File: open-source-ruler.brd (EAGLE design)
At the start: 85.5 x 54 mm, 30 parts, among them IC1 LT1007CS8, IC2 FT232RLSSOP, IC3 MDC3105DMT1, Q4 ASF1, U1 V_REG_317DPACK

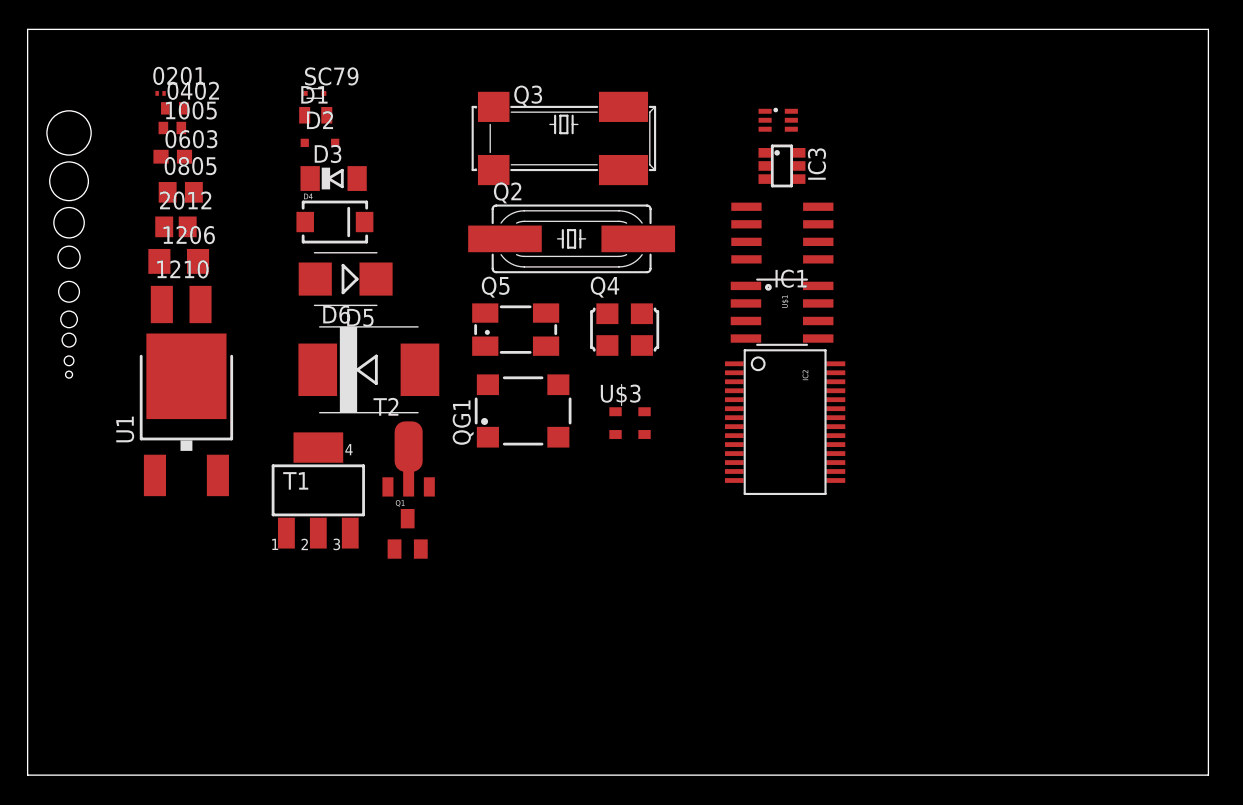
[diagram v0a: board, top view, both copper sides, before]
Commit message: Added scales
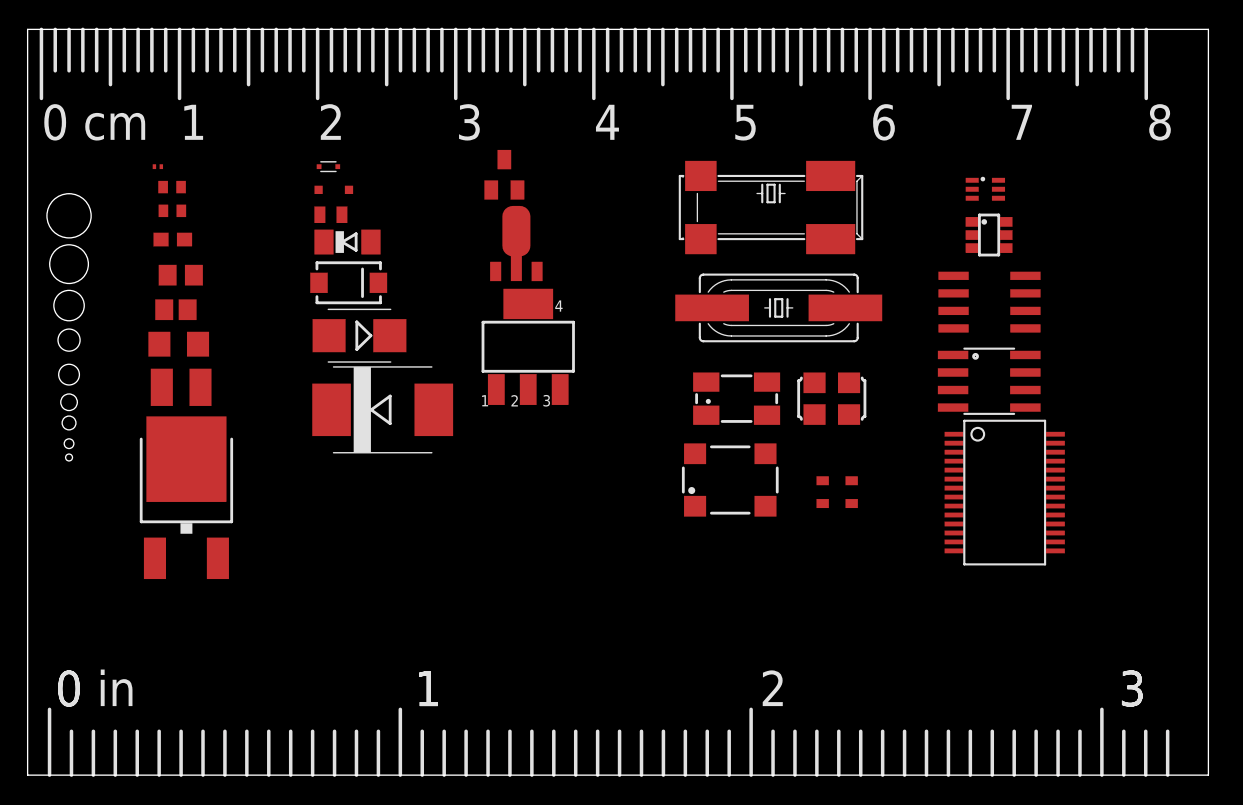
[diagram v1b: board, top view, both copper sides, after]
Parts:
- moved Q1 26.9 mm to (34.5, 43.5)
- moved T1 18.4 mm to (36.2, 31.0)
- moved T2 17.4 mm to (35.4, 38.5)
- moved Q5 16.8 mm to (51.3, 27.3)
- moved IC2 16.7 mm to (70.8, 20.5)
- moved IC1 15.8 mm to (69.7, 34.2)
- moved IC3 15.8 mm to (69.6, 39.1)
- moved Q2 15.8 mm to (54.4, 33.8)
- moved Q3 15.8 mm to (53.8, 41.1)
- moved QG1 15.8 mm to (50.9, 21.4)
- moved U$3 15.8 mm to (58.6, 20.5)
- moved Q4 15.8 mm to (58.2, 27.3)
- moved U$1 15.8 mm to (69.6, 28.5)
- moved U$2 15.8 mm to (69.3, 42.4)
- moved D1 7.28 mm to (22.0, 40.6)
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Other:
- board text added: "0"
- board text added: "1"
- board text added: "2"
- board text added: "3"
- board text added: "4"
- board text added: "5"
- board text added: "6"
- board text added: "7"
- board text added: "8"
- board text added: "cm"
- board text added: "in"

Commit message: Added prototype area
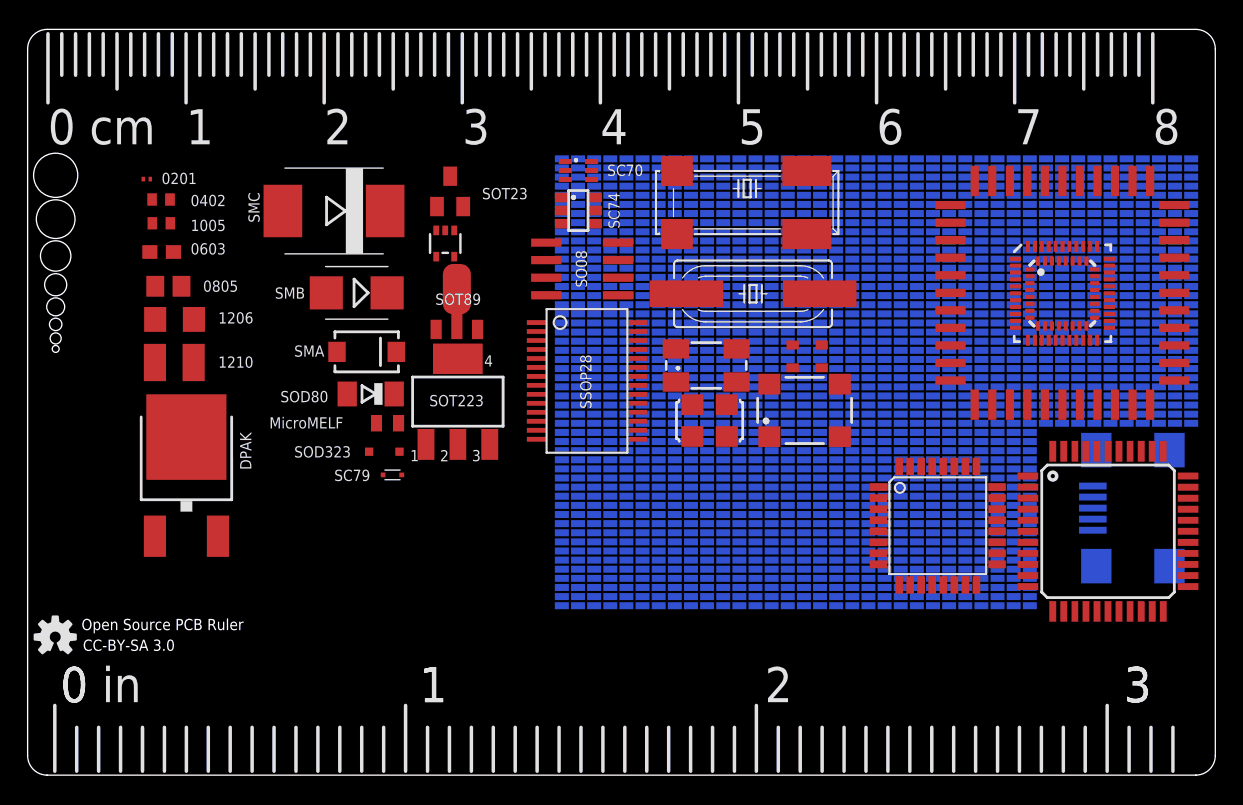
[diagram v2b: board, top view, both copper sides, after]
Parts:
- removed 2012: (no value), rcl:C2012
- added IC4: XMEGA16A4A, atmel:TQFP44
- added IC6: (no value), micro-intel:PLCC44
- added U$10, U$11, U$12, U$13, U$14, U$15, U$16, U$17, U$18, U$19, U$20, U$21, U$22, U$4, U$6, U$7, U$8, U$9: PADS, my:PADS
- added U$5: ATMEGA32U4QFN2, SparkFun:QFN-44-NOPAD
- added U2: ATMEGA168, SparkFun:TQFP32-08
- added U3: ATMEGA168MLF, SparkFun:MLF32
- added U4: 7432SE, SparkFun:SOT353
- added X1: MINI-USB-UX60A-MB-5ST, usb:UX60A-MB-5ST
- U$1: value ATTINY13SOIC -> OSHW-LOGOS; device SparkFun:SO08 -> SparkFun:OSHW-LOGO-S
- moved U$1 70.1 mm to (2.00, 10.0), turned to 0 degrees
- moved IC2 31.3 mm to (40.5, 28.5)
- moved IC3 29.8 mm to (39.9, 40.9)
- moved IC1 29.6 mm to (40.2, 36.7)
- moved U$2 29.5 mm to (39.9, 43.8)
- moved SC79 22.8 mm to (26.4, 21.7), turned to 180 degrees
- moved D2 19.3 mm to (25.8, 23.4), turned to 180 degrees
- moved D1 15.6 mm to (26.1, 25.5)
- moved D6 14.8 mm to (22.2, 40.9), turned to 180 degrees
- moved D3 11.1 mm to (24.8, 27.6), turned to 180 degrees
- moved U$3 10.1 mm to (56.4, 30.3)
- moved Q4 8.99 mm to (49.4, 25.7)
- moved QG1 7.37 mm to (56.3, 26.4)
- moved T1 6.46 mm to (31.2, 27.0)
- moved T2 6.02 mm to (31.1, 34.2)
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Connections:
- new net AVCC: IC4.39
- new net GND1: IC4.18
- new net GND2: IC4.30
- new net GND3: IC4.38
- new net VCC1: IC4.19
- new net VCC2: IC4.31
- net GND: now also IC4.8, IC6.22
- net VCC: now also IC4.9, IC6.44
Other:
- board size 85.5 x 54 mm -> 86 x 54 mm
- board text added: "0201"
- board text added: "0402"
- board text added: "0603"
- board text added: "0805"
- board text added: "1005"
- board text added: "1206"
- board text added: "1210"
- board text added: "CC-BY-SA 3.0"
- board text added: "DPAK"
- board text added: "MicroMELF"
- board text added: "Open Source PCB Ruler"
- board text added: "SC70"
- board text added: "SC74"
- board text added: "SC79"
- board text added: "SMA"
- board text added: "SMB"
- board text added: "SMC"
- board text added: "SO08"
- board text added: "SOD323"
- board text added: "SOD80"
- board text added: "SOT223"
- board text added: "SOT23"
- board text added: "SOT89"
- board text added: "SSOP28"

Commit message: +trace,colour,few FPs
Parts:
- added S1: SWITCH-MOMENTARY-2, SparkFun:TACTILE_SWITCH_TALL
- added U$23, U$24: PADS, my:PADS
- added U$25: HMC5883LSMD, SparkFun:16LPCC
- added U$26: U.FL, SparkFun:U.FL
- moved U3 3.41 mm to (78.0, 33.4)
- moved U$5 3.30 mm to (77.9, 33.4), turned to 90 degrees
- moved X1 2.41 mm to (79.4, 16.9)
- moved Q4 2.13 mm to (48.7, 23.6)
- moved QG1 2.05 mm to (56.5, 24.4)
- moved U$20 2.04 mm to (43.8, 26.4)
- moved U$21 2.04 mm to (43.8, 19.8)
- moved U$22 2.04 mm to (43.8, 13.2)
- moved U$12 2.04 mm to (67.2, 26.4)
- moved U$13 2.04 mm to (67.2, 19.8)
- moved U$14 2.04 mm to (55.5, 19.8)
- moved U$15 2.04 mm to (55.5, 26.4)
- moved U$4 2.04 mm to (67.2, 13.2)
- moved U$8 2.04 mm to (78.9, 26.4)
- moved U$9 2.04 mm to (55.5, 13.2)
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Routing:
- net N$1: track 0.00 -> 7.98 mm
- net N$2: track 0.00 -> 7.92 mm
- net N$3: track 0.00 -> 7.87 mm
- net N$4: track 0.00 -> 7.82 mm
- net N$5: track 0.00 -> 7.67 mm
- net N$6: track 0.00 -> 7.52 mm
- net N$7: track 0.00 -> 7.37 mm
- net N$8: track 0.00 -> 7.11 mm
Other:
- board text added: "-12"
- board text added: "-3"
- board text added: "-6"
- board text added: "-9"
- board text added: "0 1 2 3 4 5 6 7 8 9"
- board text added: "10"
- board text added: "12"
- board text added: "18"
- board text added: "24"
- board text added: "30"
- board text added: "40"
- board text added: "86SMX"
- board text added: "9"
- board text added: "ASE"
- board text added: "ASF"
- board text added: "CTS406"
- board text added: "Colour Code BLACK BROWN RED ORANGE YELLOW GREEN BLUE VIOLET GRAY WHITE"
- board text added: "GIGA"
- board text added: "HC49UP"
- board text added: "KILO"
- board text added: "MEGA"
- board text added: "MLF32"
- board text added: "PREFIXES"
- board text added: "QFN44"
- board text added: "QFP32-08"
- board text added: "QFP44-08"
- board text added: "SC 74"
- board text added: "SM77H"
- board text added: "SOT353"
- board text added: "TACT-SW"
- board text added: "TERA"
- board text added: "Trace Width(mil)"
- board text added: "U.FL"
- board text added: "micro"
- board text added: "milli"
- board text added: "nano"
- board text added: "pico"
- board text removed: "SC74"

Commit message: Ready for release
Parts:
- removed T1: (no value), transistor-neu-to92:SOT223
- removed T2: (no value), transistor-neu-to92:SOT89-BCE
- added IC5: LFXP20E_XXF256, lattice:FPBGA_256
- added IC7: ADSP_BF531, analog-devices:MBGA_160
- added IC8: (no value), SparkFun:SOT223
- added Q6: (no value), SparkFun:SOT89
- moved U$26 9.66 mm to (46.1, 12.4)
- moved U$3 4.69 mm to (60.4, 27.8)
- moved U2 4.45 mm to (66.2, 13.6)
- moved S1 4.16 mm to (55.2, 13.3)
- moved QG1 3.32 mm to (58.9, 22.1)
- moved Q3 3.14 mm to (54.4, 39.3)
- moved Q2 3.05 mm to (54.7, 32.7)
- moved Q4 2.57 mm to (49.6, 21.2)
- moved Q5 2.56 mm to (50.3, 27.4)
- moved U$2 2.50 mm to (41.4, 41.8)
- moved IC3 2.44 mm to (41.4, 38.7)
- moved IC4 2.42 mm to (78.1, 15.2)
- moved IC1 2.33 mm to (41.4, 34.5)
- moved IC2 2.33 mm to (41.4, 26.4)
- moved U4 2.33 mm to (31.6, 37.3)
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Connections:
- new net CLKIN: IC7.A12
- new net EMU_B: IC7.M2
- new net GNDP0: IC5.H5
- new net GNDP1: IC5.J13
- new net RTXI: IC7.A9
- new net RTXO: IC7.A8
- new net VCCAUX: IC5.E13, IC5.E4, IC5.M13, IC5.M4
- new net VCCIO0: IC5.F7, IC5.F8
- new net VCCIO1: IC5.F10, IC5.F9
- new net VCCIO2: IC5.G11, IC5.H11
- new net VCCIO3: IC5.J11, IC5.K11
- new net VCCIO4: IC5.L10, IC5.L9
- new net VCCIO5: IC5.L7, IC5.L8
- new net VCCIO6: IC5.J6, IC5.K6
- new net VCCIO7: IC5.G6, IC5.H6
- new net VCCJ: IC5.D16
- new net VCCP0: IC5.H4
- new net VCCP1: IC5.J12
- new net VDD_EXT: IC7.A1, IC7.C12, IC7.C7, IC7.D5, IC7.D9, IC7.F12, IC7.G4, IC7.J12, IC7.J4, IC7.L11, IC7.L7, IC7.P1
- new net VDD_INT: IC7.D6, IC7.E11, IC7.E4, IC7.J11, IC7.L4, IC7.L9
- new net VDD_RTC: IC7.B9
- new net VROUT: IC7.A13, IC7.B12
- new net XTAL: IC7.A11
- net GND: now also IC5.A1, IC5.A16, IC5.F11, IC5.F6, IC5.G10, IC5.G7, IC5.G8, IC5.G9, IC5.H10, IC5.H7, IC5.H8, IC5.H9, IC5.J10, IC5.J7, IC5.J8, IC5.J9, IC5.K10, IC5.K7, IC5.K8, IC5.K9, IC5.L11, IC5.L6, IC5.T1, IC5.T16, IC7.A10, IC7.A14, IC7.B11, IC7.C11, IC7.C4, IC7.C5, IC7.D10, IC7.D11, IC7.D4, IC7.D7, IC7.D8, IC7.F11, IC7.F4, IC7.G11, IC7.H11, IC7.H4, IC7.K11, IC7.K4, IC7.L10, IC7.L5, IC7.L6, IC7.L8, IC7.M10, IC7.P14
- net VCC: now also IC5.D13, IC5.D4, IC5.E12, IC5.E5, IC5.M12, IC5.M5, IC5.N13, IC5.N4
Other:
- board text added: "11"
- board text added: "13"
- board text added: "14"
- board text added: "15"
- board text added: "16"
- board text added: "17"
- board text added: "20"
- board text added: "21"
- board text added: "22"
- board text added: "23"
- board text added: "25"
- board text added: "AWG"
- board text added: "FBGA-256"
- board text added: "LPCC16"
- board text added: "MBGA-160"
- board text added: "SC 70"
- board text added: "SOT 353"
- board text removed: "SC70"
- board text removed: "SOT353"

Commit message: Ready to prototype
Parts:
- removed U$1: OSHW-LOGOS, SparkFun:OSHW-LOGO-S
- added D7: (no value), diode:MELF-MLL41
- added D8: (no value), diode:MINIMELF
- added IC9: (no value), linear:TO263-5
- added U$27: LOGO_SMALL, my:LOGO_SMALL
- added U$28: OSHW-LOGOM, SparkFun:OSHW-LOGO-M
- moved D3 7.11 mm to (24.4, 19.4)
- moved D2 4.70 mm to (25.4, 17.3)
- moved SC79 4.32 mm to (25.9, 15.4)
- moved D1 2.85 mm to (25.6, 21.4), turned to 180 degrees
- moved U$26 2.54 mm to (48.6, 12.3)
- moved S1 0.64 mm to (55.9, 13.3)
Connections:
- net GND: now also IC9.3, IC9.6
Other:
- board text added: "MELF"
- board text added: "MiniMELF"
- board text added: "TO263"

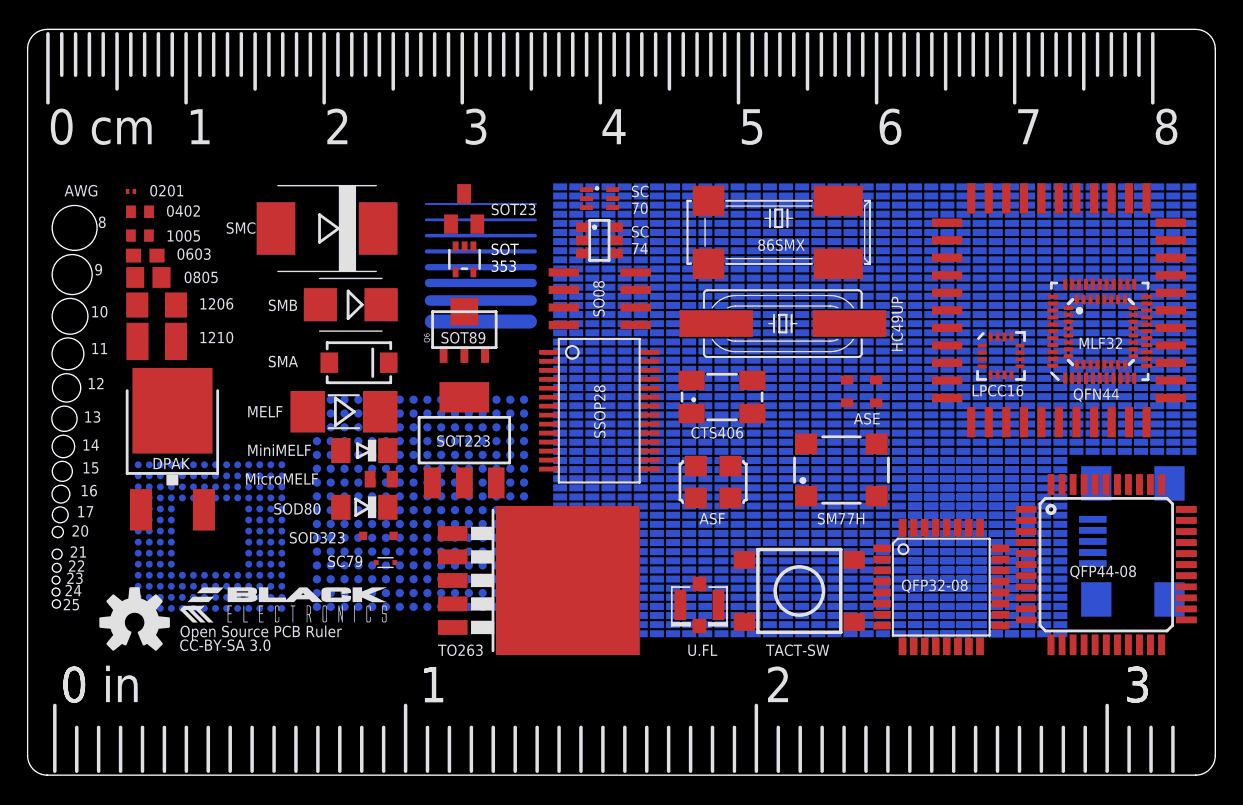
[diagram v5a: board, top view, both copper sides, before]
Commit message: Fixed Issues #1-#4
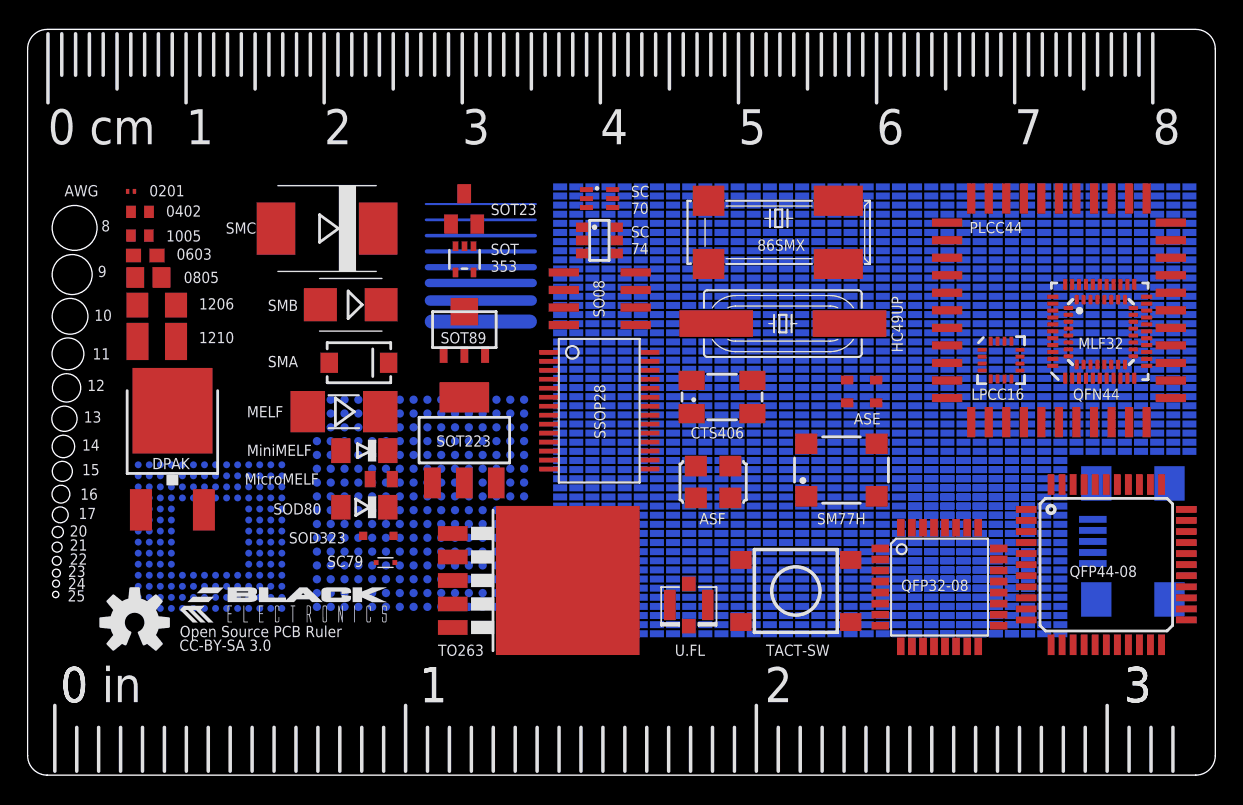
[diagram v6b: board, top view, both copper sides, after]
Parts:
- moved U$26 0.76 mm to (47.9, 12.3)
- moved U$25 0.30 mm to (70.5, 30.0)
- moved S1 0.25 mm to (55.6, 13.3)
- moved U2 0.13 mm to (66.0, 13.6)
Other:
- board text added: "MINI-USB"
- board text added: "PLCC44"
